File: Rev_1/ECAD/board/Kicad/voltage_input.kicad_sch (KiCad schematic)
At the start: 22 parts, among them Q1 PMOS, Q2 PNP, Q3 PNP, U200 USB_C_6PIN, U202 FT232RL, U4 L7805ABV

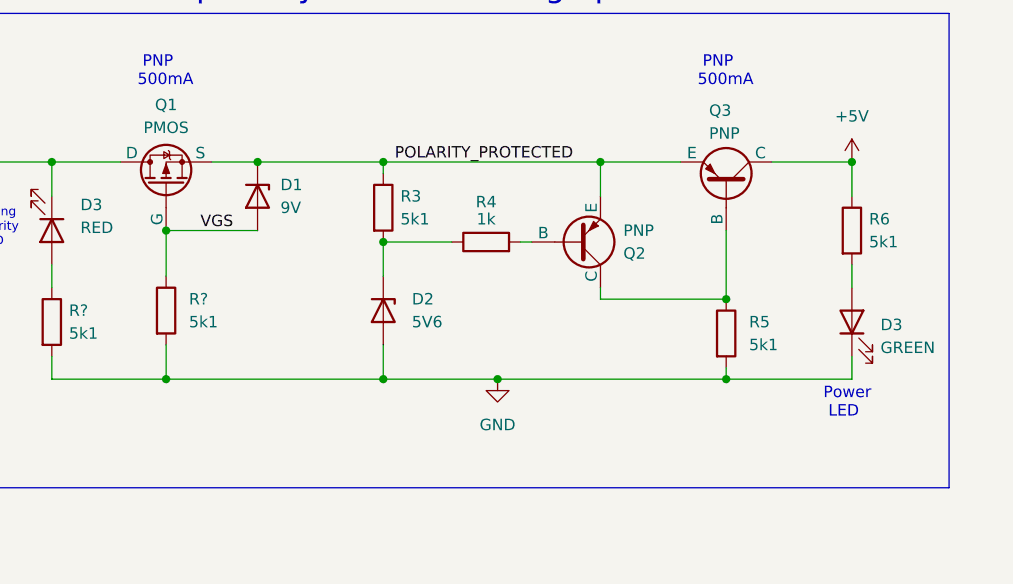
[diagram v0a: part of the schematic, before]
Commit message: Changed from 4-bit registers to shift registers
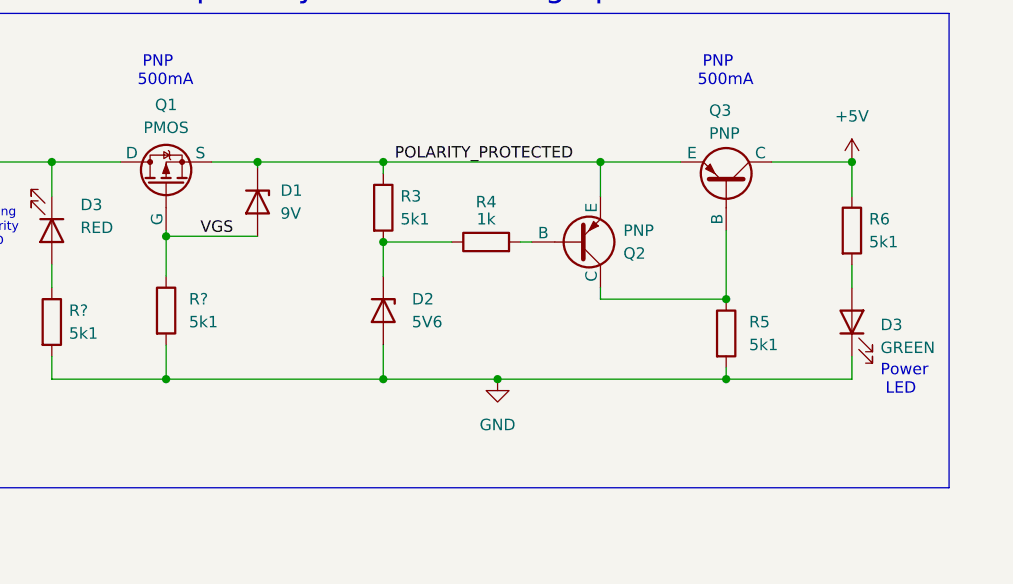
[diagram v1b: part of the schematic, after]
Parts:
- D1, D2: footprint Package_TO_SOT_SMD:SOT-23 -> Diode_SMD:D_0805_2012Metric_Pad1.15x1.40mm_HandSolder
- JP2: footprint Jumper:SolderJumper-3_P1.3mm_Open_Pad1.0x1.5mm -> Jumper:SolderJumper-2_P1.3mm_Open_RoundedPad1.0x1.5mm
- Q1: footprint (none) -> Package_TO_SOT_THT:TO-92
- U200: footprint (none) -> EEPROM_PROGRAMMER:USB_C_6PIN
- U201: footprint (none) -> EEPROM_PROGRAMMER:Battery_Connectors
- U202: footprint (none) -> EEPROM_PROGRAMMER:FT232RL
- U4: footprint (none) -> EEPROM_PROGRAMMER:L7805ABV
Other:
- moved on the sheet: D1
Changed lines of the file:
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@@
   (junction (at 158.115 93.98) (diameter 0) (color 0 0 0 0)
   )
-  (junction (at 170.815 101.6) (diameter 0) (color 0 0 0 0)
-  )
   (junction (at 194.945 102.87) (diameter 0) (color 0 0 0 0)
   )
@@
   )
   (junction (at 247.015 93.98) (diameter 0) (color 0 0 0 0)
+  )
+  (junction (at 170.815 102.235) (diameter 0) (color 0 0 0 0)
   )
   (no_connect (at 40.64 142.24))
@@
     (stroke (width 0) (type default))
   )
-  (wire (pts (xy 170.815 106.68) (xy 170.815 101.6))
+  (wire (pts (xy 170.815 106.68) (xy 170.815 102.235))
     (stroke (width 0) (type default))
   )
@@
     (stroke (width 0) (type default))
   )
+  (wire (pts (xy 170.815 102.235) (xy 170.815 101.6))
+    (stroke (width 0) (type default))
+  )
   (wire (pts (xy 127 78.105) (xy 127 81.28))
     (stroke (width 0) (type default))
@@
     (stroke (width 0) (type default))
   )
+  (wire (pts (xy 180.975 94.615) (xy 180.975 93.98))
+    (stroke (width 0) (type default))
+  )
   (wire (pts (xy 219.075 109.22) (xy 233.045 109.22))
     (stroke (width 0) (type default))
@@
     (stroke (width 0) (type default))
   )
-  (wire (pts (xy 170.815 101.6) (xy 180.975 101.6))
+  (wire (pts (xy 170.815 102.235) (xy 180.975 102.235))
     (stroke (width 0) (type default))
   )
@@
     (effects (font (size 1.27 1.27)) (justify left bottom))
   )
-  (text "Power\n LED" (at 243.84 122.555 0)
+  (text "Power\n LED" (at 250.19 120.015 0)
     (effects (font (size 1.27 1.27)) (justify left bottom))
   )
@@
     (effects (font (size 1.27 1.27)) (justify left bottom))
   )
-  (label "VGS" (at 174.625 101.6 0) (fields_autoplaced)
+  (label "VGS" (at 174.625 102.235 0) (fields_autoplaced)
     (effects (font (size 1.27 1.27)) (justify left bottom))
   )
@@
       (effects (font (size 1.27 1.27)))
     )
-    (property "Footprint" "" (at 35.56 50.8 90)
+    (property "Footprint" "EEPROM_PROGRAMMER:USB_C_6PIN" (at 35.56 50.8 90)
       (effects (font (size 1.27 1.27)) hide)
     )
@@
       (effects (font (size 1.27 1.27)))
     )
-    (property "Footprint" "" (at 168.275 91.44 0)
+    (property "Footprint" "Package_TO_SOT_THT:TO-92" (at 168.275 91.44 0)
       (effects (font (size 1.27 1.27)) hide)
     )
@@
     )
   )
-  (symbol (lib_id "Device:D_Zener") (at 180.975 97.79 270) (unit 1)
-    (in_bom yes) (on_board yes) (dnp no) (fields_autoplaced)
-    (property "Reference" "D1" (at 183.515 96.52 90)
-      (effects (font (size 1.27 1.27)) (justify left))
-    )
-    (property "Value" "9V" (at 183.515 99.06 90)
-      (effects (font (size 1.27 1.27)) (justify left))
-    )
-    (property "Footprint" "Package_TO_SOT_SMD:SOT-23" (at 180.975 97.79 0)
-      (effects (font (size 1.27 1.27)) hide)
-    )
-    (property "Datasheet" "~" (at 180.975 97.79 0)
+  (symbol (lib_id "Device:D_Zener") (at 180.975 98.425 270) (unit 1)
+    (in_bom yes) (on_board yes) (dnp no) (fields_autoplaced)
+    (property "Reference" "D1" (at 183.515 97.155 90)
+      (effects (font (size 1.27 1.27)) (justify left))
+    )
+    (property "Value" "9V" (at 183.515 99.695 90)
+      (effects (font (size 1.27 1.27)) (justify left))
+    )
+    (property "Footprint" "Diode_SMD:D_0805_2012Metric_Pad1.15x1.40mm_HandSolder" (at 180.975 98.425 0)
+      (effects (font (size 1.27 1.27)) hide)
+    )
+    (property "Datasheet" "~" (at 180.975 98.425 0)
       (effects (font (size 1.27 1.27)) hide)
     )
@@
     )
   )
-  (symbol (lib_name "FT232RL_1") (lib_id "EEPROM_PROGRAMMER:FT232RL") (at 35.56 138.43 90) (unit 1)
+  (symbol (lib_id "EEPROM_PROGRAMMER:FT232RL") (at 35.56 138.43 90) (unit 1)
     (in_bom yes) (on_board yes) (dnp no) (fields_autoplaced)
     (property "Reference" "U202" (at 35.56 126.365 90)
@@
       (effects (font (size 1.27 1.27)))
     )
-    (property "Footprint" "" (at 35.56 138.43 0)
+    (property "Footprint" "EEPROM_PROGRAMMER:FT232RL" (at 35.56 138.43 0)
       (effects (font (size 1.27 1.27)) hide)
     )
@@
       (effects (font (size 1.27 1.27)))
     )
-    (property "Footprint" "" (at 34.29 95.25 0)
+    (property "Footprint" "EEPROM_PROGRAMMER:Battery_Connectors" (at 34.29 95.25 0)
       (effects (font (size 1.27 1.27)) hide)
     )
@@
     )
   )
-  (symbol (lib_name "L7805ABV_1") (lib_id "EEPROM_PROGRAMMER:L7805ABV") (at 64.77 95.25 0) (unit 1)
+  (symbol (lib_id "EEPROM_PROGRAMMER:L7805ABV") (at 64.77 95.25 0) (unit 1)
     (in_bom yes) (on_board yes) (dnp no) (fields_autoplaced)
     (property "Reference" "U4" (at 64.77 88.265 0)
@@
       (effects (font (size 1.27 1.27)))
     )
-    (property "Footprint" "" (at 64.77 93.98 0)
+    (property "Footprint" "EEPROM_PROGRAMMER:L7805ABV" (at 64.77 93.98 0)
       (effects (font (size 1.27 1.27)) hide)
     )
@@
       (effects (font (size 1.27 1.27)) (justify right) hide)
     )
-    (property "Footprint" "Jumper:SolderJumper-3_P1.3mm_Open_Pad1.0x1.5mm" (at 127 85.09 0)
+    (property "Footprint" "Jumper:SolderJumper-2_P1.3mm_Open_RoundedPad1.0x1.5mm" (at 127 85.09 0)
       (effects (font (size 1.27 1.27)) hide)
     )
@@
       (effects (font (size 1.27 1.27)) (justify left))
     )
-    (property "Footprint" "Package_TO_SOT_SMD:SOT-23" (at 194.945 110.49 0)
-      (effects (font (size 1.27 1.27)) hide)
-    )
+    (property "Footprint" "Diode_SMD:D_0805_2012Metric_Pad1.15x1.40mm_HandSolder" (at 194.945 110.49 0)
+      (effects (font (size 1.27 1.27)) hide)
+    )

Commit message: Made a ruf idea of the input protection on the pcb
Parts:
- renumbered U4 to U203
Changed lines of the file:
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@@
   (symbol (lib_id "EEPROM_PROGRAMMER:L7805ABV") (at 64.77 95.25 0) (unit 1)
     (in_bom yes) (on_board yes) (dnp no) (fields_autoplaced)
-    (property "Reference" "U4" (at 64.77 88.265 0)
+    (property "Reference" "U203" (at 64.77 87.63 0)
       (effects (font (size 1.27 1.27)))
     )
-    (property "Value" "L7805ABV" (at 64.77 90.805 0)
+    (property "Value" "L7805ABV" (at 64.77 90.17 0)
       (effects (font (size 1.27 1.27)))
     )
@@
       (project "board"
         (path "/2f4d49fd-9c63-4eb5-a266-4b5553b3e489/86ee93c3-557f-4dc7-a98b-7b4dc8a79ba7"
-          (reference "U4") (unit 1)
+          (reference "U203") (unit 1)
         )
       )

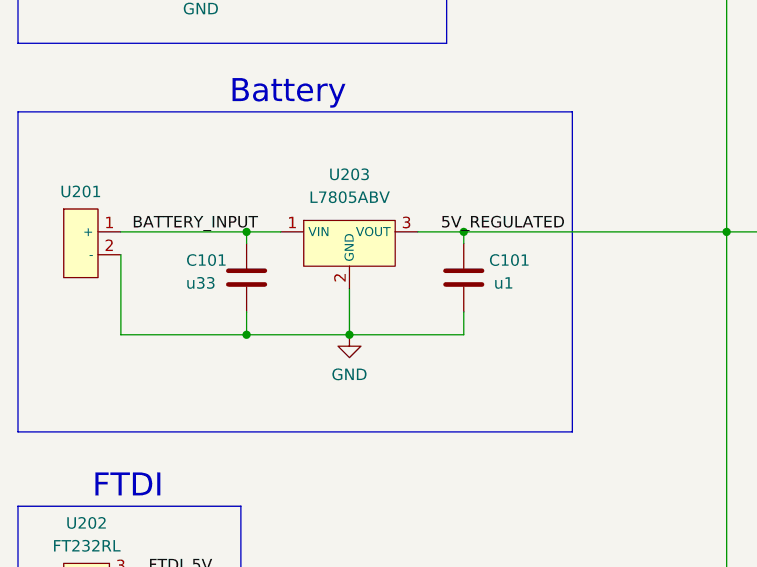
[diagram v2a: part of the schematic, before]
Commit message: Changed the footprint on D201 and D202 to DO-35_SOD27
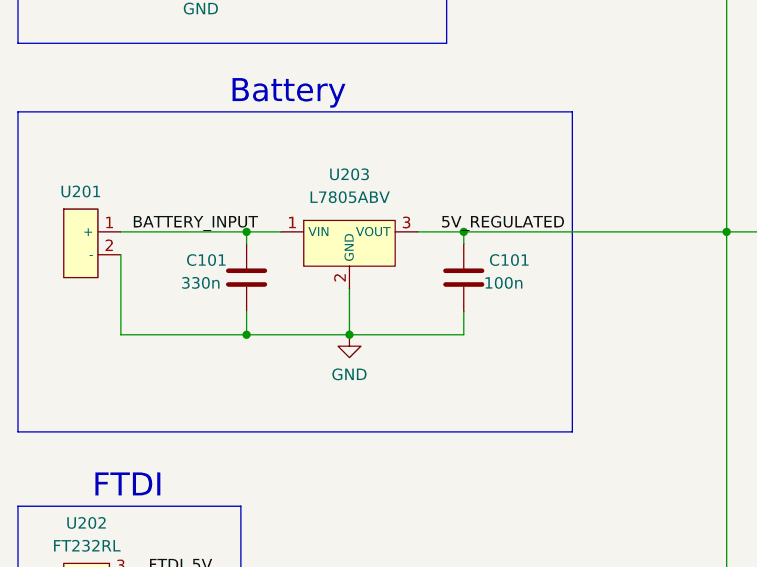
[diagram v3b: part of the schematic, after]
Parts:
- C101: value u33 -> 330n
- C101: value u1 -> 100n
- D1, D2: footprint Diode_SMD:D_0805_2012Metric_Pad1.15x1.40mm_HandSolder -> Diode_THT:D_DO-35_SOD27_P3.81mm_Vertical_KathodeUp
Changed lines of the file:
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@@
       (effects (font (size 1.27 1.27)))
     )
-    (property "Value" "u33" (at 48.26 99.695 0)
+    (property "Value" "330n" (at 48.26 99.695 0)
       (effects (font (size 1.27 1.27)))
     )
@@
       (effects (font (size 1.27 1.27)) (justify left))
     )
-    (property "Footprint" "Diode_SMD:D_0805_2012Metric_Pad1.15x1.40mm_HandSolder" (at 180.975 98.425 0)
+    (property "Footprint" "Diode_THT:D_DO-35_SOD27_P3.81mm_Vertical_KathodeUp" (at 180.975 98.425 0)
       (effects (font (size 1.27 1.27)) hide)
     )
@@
       (effects (font (size 1.27 1.27)))
     )
-    (property "Value" "u1" (at 81.915 99.695 0)
+    (property "Value" "100n" (at 81.915 99.695 0)
       (effects (font (size 1.27 1.27)))
     )
@@
       (effects (font (size 1.27 1.27)) (justify left))
     )
-    (property "Footprint" "Diode_SMD:D_0805_2012Metric_Pad1.15x1.40mm_HandSolder" (at 194.945 110.49 0)
-      (effects (font (size 1.27 1.27)) hide)
-    )
+    (property "Footprint" "Diode_THT:D_DO-35_SOD27_P3.81mm_Vertical_KathodeUp" (at 194.945 110.49 0)
+      (effects (font (size 1.27 1.27)) hide)
+    )

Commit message: Everything finished, can start routing
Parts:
- Q1: footprint Package_TO_SOT_THT:TO-92 -> Package_TO_SOT_SMD:SOT-23
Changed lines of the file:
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@@
       (effects (font (size 1.27 1.27)))
     )
-    (property "Footprint" "Package_TO_SOT_THT:TO-92" (at 168.275 91.44 0)
+    (property "Footprint" "Package_TO_SOT_SMD:SOT-23" (at 168.275 91.44 0)
       (effects (font (size 1.27 1.27)) hide)
     )
-    (property "Datasheet" "https://ngspice.sourceforge.io/docs/ngspice-manual.pdf" (at 183.515 96.52 0)
+    (property "Datasheet" "" (at 183.515 96.52 0)
       (effects (font (size 1.27 1.27)) hide)
     )
